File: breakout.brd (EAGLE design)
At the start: 38.1 x 21.9 mm, 5 parts

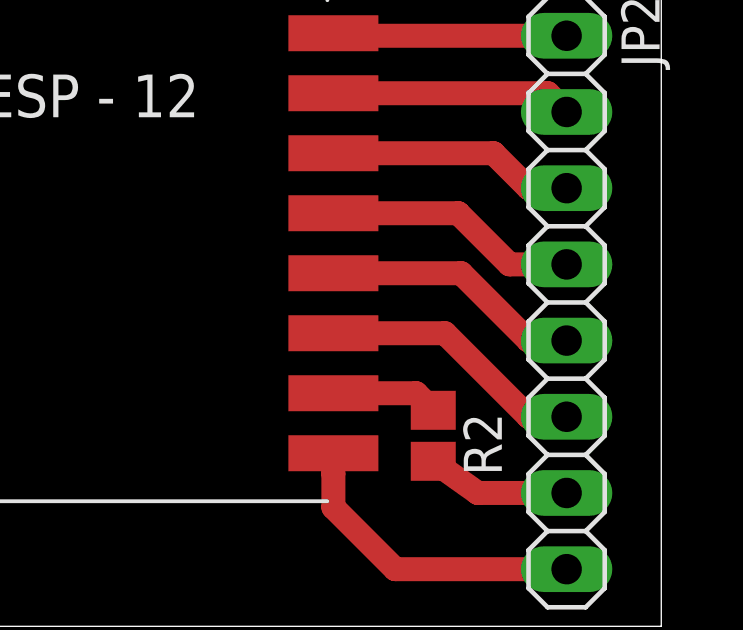
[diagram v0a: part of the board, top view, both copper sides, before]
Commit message: Added GPIO0 resistor
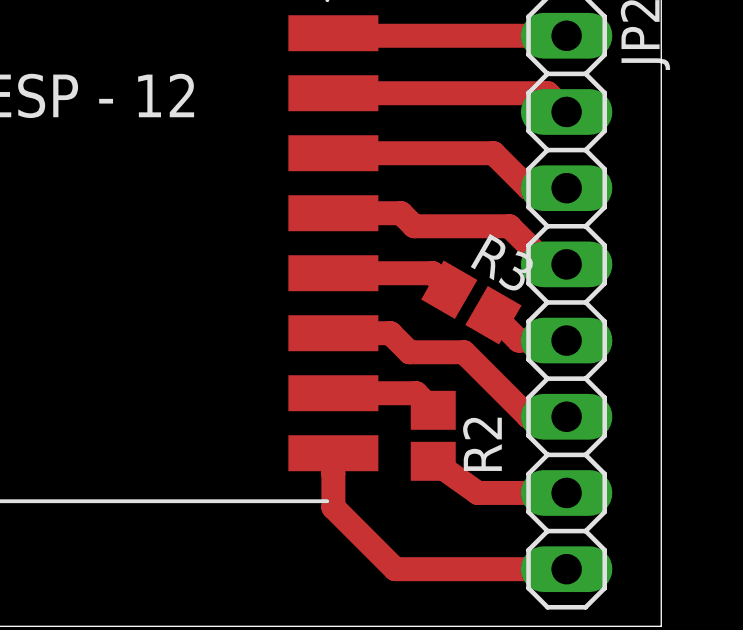
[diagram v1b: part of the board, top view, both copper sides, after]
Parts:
- added R3: (no value), resistor:R0805
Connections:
- new net N$19: JP2.5, R3.2
- net N$13: now also R3.1; no longer JP2.5
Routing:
- net N$13: track 8.70 -> 4.09 mm
- net N$19: track 0.00 -> 2.79 mm
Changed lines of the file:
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@@
 <attribute name="VALUE" x="28.194" y="9.017" size="1.27" layer="27" rot="R270"/>
+</element>
+<element name="R3" library="resistor" package="R0805" value="" x="31.75" y="12.7" rot="R330">
+<attribute name="NAME" x="31.59809375" y="13.960871875" size="1.27" layer="25" rot="R330"/>
+<attribute name="VALUE" x="29.947103125" y="11.1012625" size="1.27" layer="27" rot="R330"/>
 </element>
 </elements>
@@
 <contactref element="U1" pad="GPIO5"/>
 <contactref element="JP2" pad="4"/>
-<wire x1="27.15" y1="15.675" x2="31.315" y2="15.675" width="0.8" layer="1"/>
-<wire x1="31.315" y1="15.675" x2="33.02" y2="13.97" width="0.8" layer="1"/>
-<wire x1="33.02" y1="13.97" x2="34.925" y2="13.97" width="0.8" layer="1"/>
-</signal>
-<signal name="N$13">
-<contactref element="U1" pad="GPIO0"/>
-<contactref element="JP2" pad="5"/>
-<wire x1="27.15" y1="13.675" x2="31.41" y2="13.675" width="0.8" layer="1"/>
-<wire x1="33.655" y1="11.43" x2="34.925" y2="11.43" width="0.8" layer="1"/>
-<wire x1="31.41" y1="13.675" x2="33.655" y2="11.43" width="0.8" layer="1"/>
+<wire x1="27.15" y1="15.675" x2="29.41" y2="15.675" width="0.8" layer="1"/>
+<wire x1="29.845" y1="15.24" x2="29.41" y2="15.675" width="0.8" layer="1"/>
+<wire x1="34.29" y1="13.97" x2="34.925" y2="13.97" width="0.8" layer="1"/>
+<wire x1="34.29" y1="13.97" x2="33.02" y2="15.24" width="0.8" layer="1"/>
+<wire x1="33.02" y1="15.24" x2="29.845" y2="15.24" width="0.8" layer="1"/>
 </signal>
 <signal name="N$14">
 <contactref element="U1" pad="GPIO2"/>
 <contactref element="JP2" pad="6"/>
-<wire x1="27.15" y1="11.675" x2="30.87" y2="11.675" width="0.8" layer="1"/>
+<wire x1="31.505" y1="11.04" x2="29.69" y2="11.04" width="0.8" layer="1"/>
+<wire x1="29.69" y1="11.04" x2="29.055" y2="11.675" width="0.8" layer="1"/>
+<wire x1="27.15" y1="11.675" x2="29.055" y2="11.675" width="0.8" layer="1"/>
 <wire x1="33.655" y1="8.89" x2="34.925" y2="8.89" width="0.8" layer="1"/>
-<wire x1="30.87" y1="11.675" x2="33.655" y2="8.89" width="0.8" layer="1"/>
+<wire x1="31.505" y1="11.04" x2="33.655" y2="8.89" width="0.8" layer="1"/>
 </signal>
 <signal name="N$16">
@@
 <wire x1="29.91" y1="9.675" x2="27.15" y2="9.675" width="0.8" layer="1"/>
 </signal>
+<signal name="N$13">
+<contactref element="U1" pad="GPIO0"/>
+<contactref element="R3" pad="1"/>
+<wire x1="31.013878125" y1="13.125" x2="30.463878125" y2="13.675" width="0.8" layer="1"/>
+<wire x1="30.463878125" y1="13.675" x2="27.15" y2="13.675" width="0.8" layer="1"/>
+</signal>
+<signal name="N$19">
+<contactref element="JP2" pad="5"/>
+<contactref element="R3" pad="2"/>
+<wire x1="32.48611875" y1="12.275" x2="33.33111875" y2="11.43" width="0.8" layer="1"/>
+<wire x1="33.33111875" y1="11.43" x2="34.925" y2="11.43" width="0.8" layer="1"/>
+</signal>
 </signals>

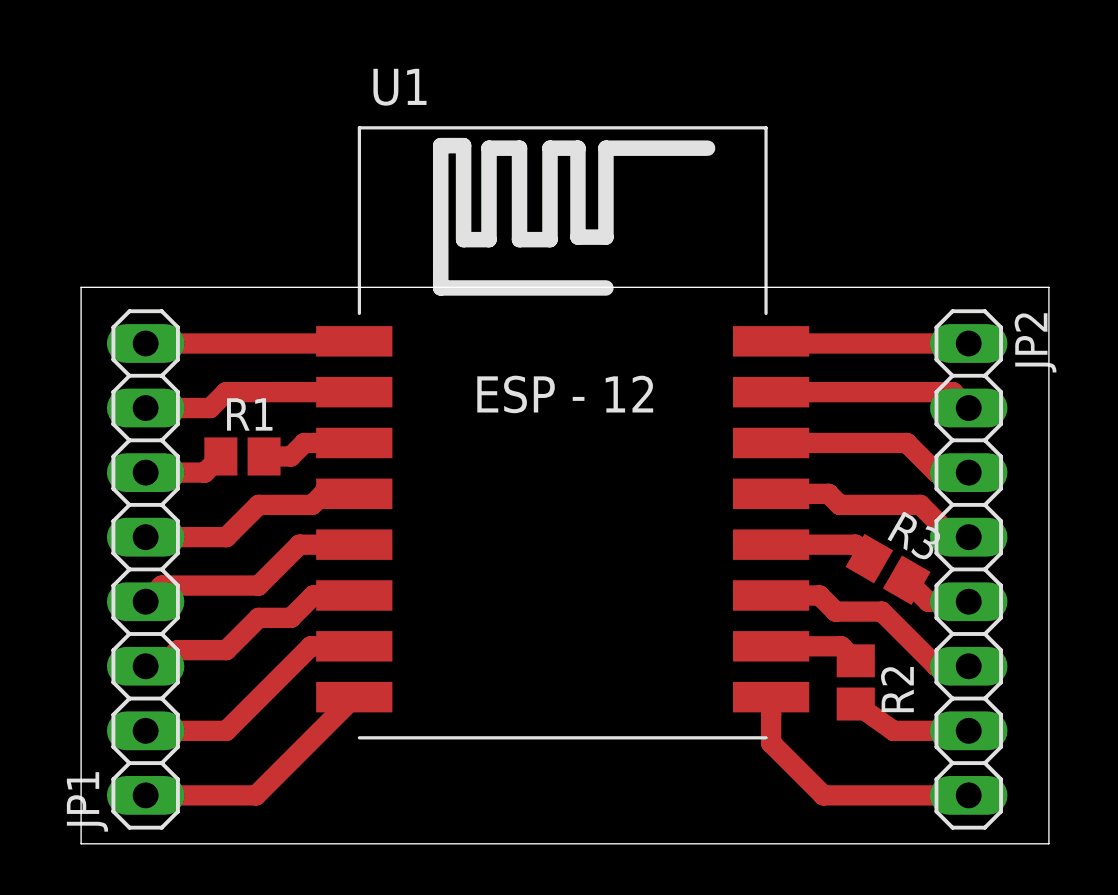
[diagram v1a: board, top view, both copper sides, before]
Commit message: Modified pads, changed traces width and gcode options
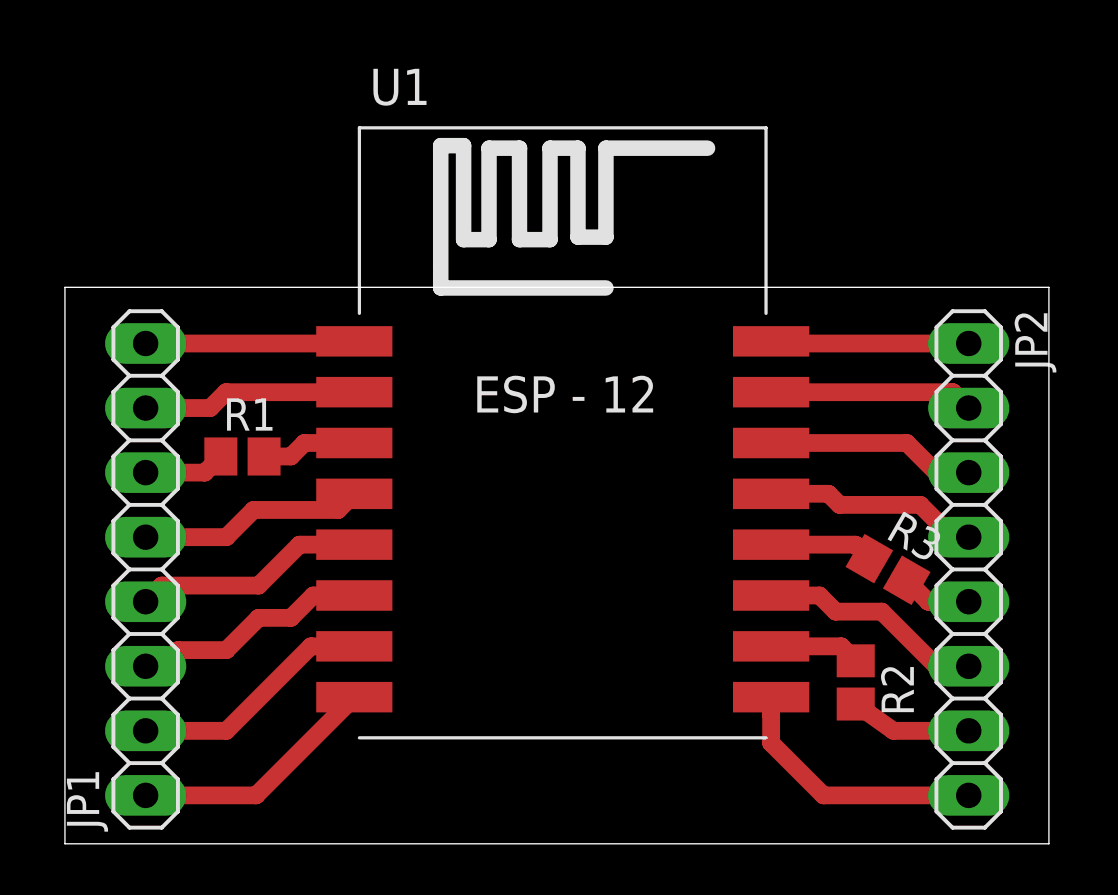
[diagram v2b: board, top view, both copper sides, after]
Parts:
- JP1, JP2: device pinhead:1X08 -> pinhead-1:1X08
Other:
- board size 38.1 x 21.9 mm -> 38.7 x 21.9 mm
